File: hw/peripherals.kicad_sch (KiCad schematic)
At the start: 10 parts, among them J4 Expansion, Q2 RU1J002YN, U8 RV-3129-C3, U9 PCA9536D

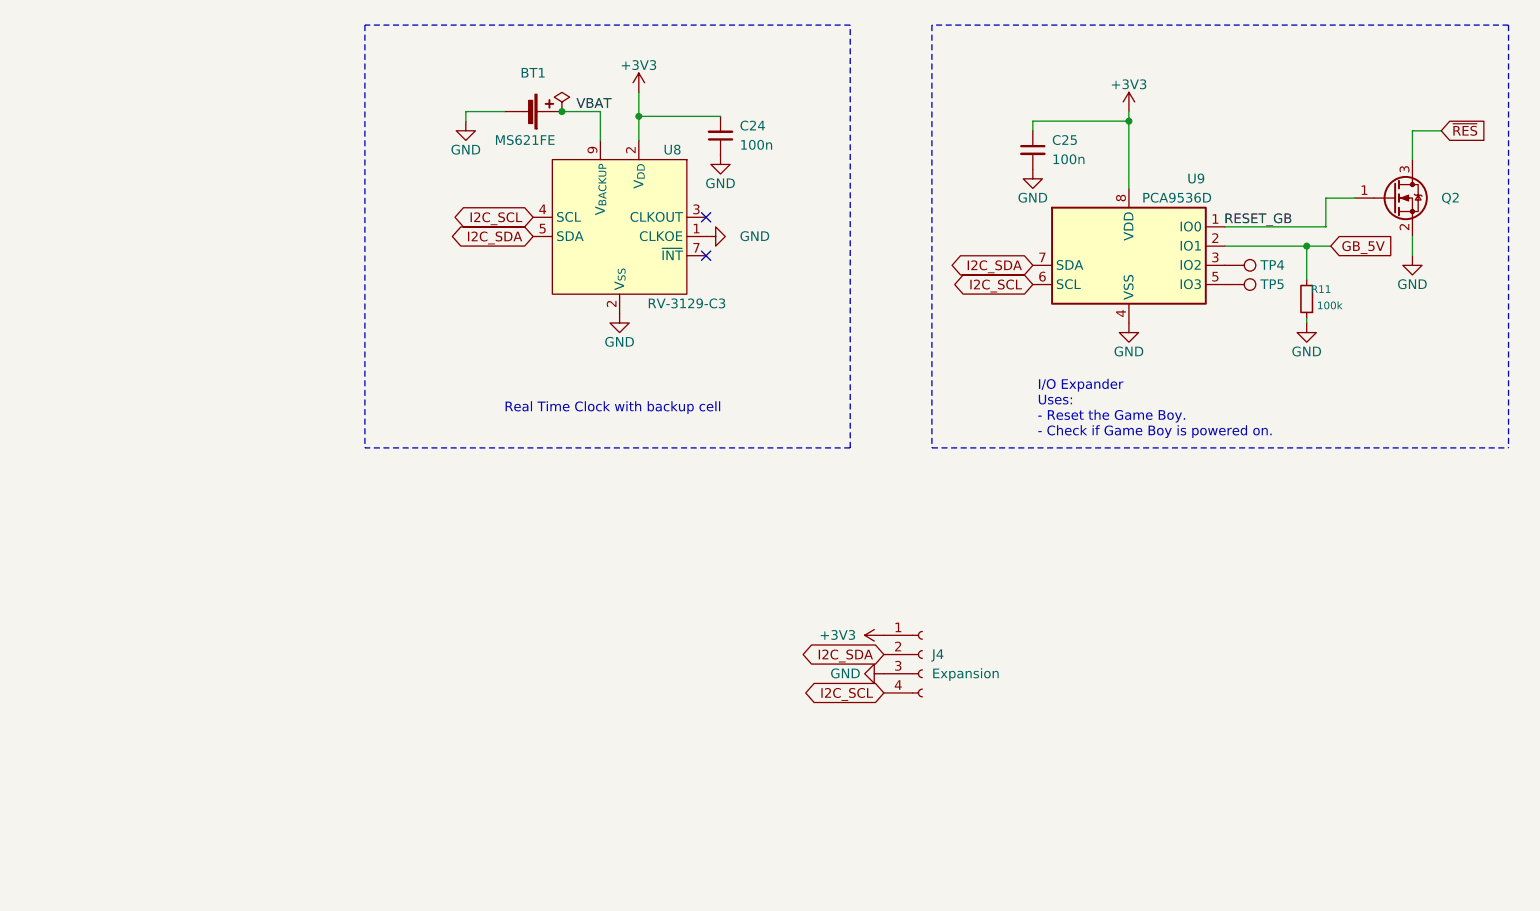
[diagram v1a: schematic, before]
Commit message: hw: use parts from LCSC
Signed-off-by: Mahyar Koshkouei <mk@deltabeard.com>
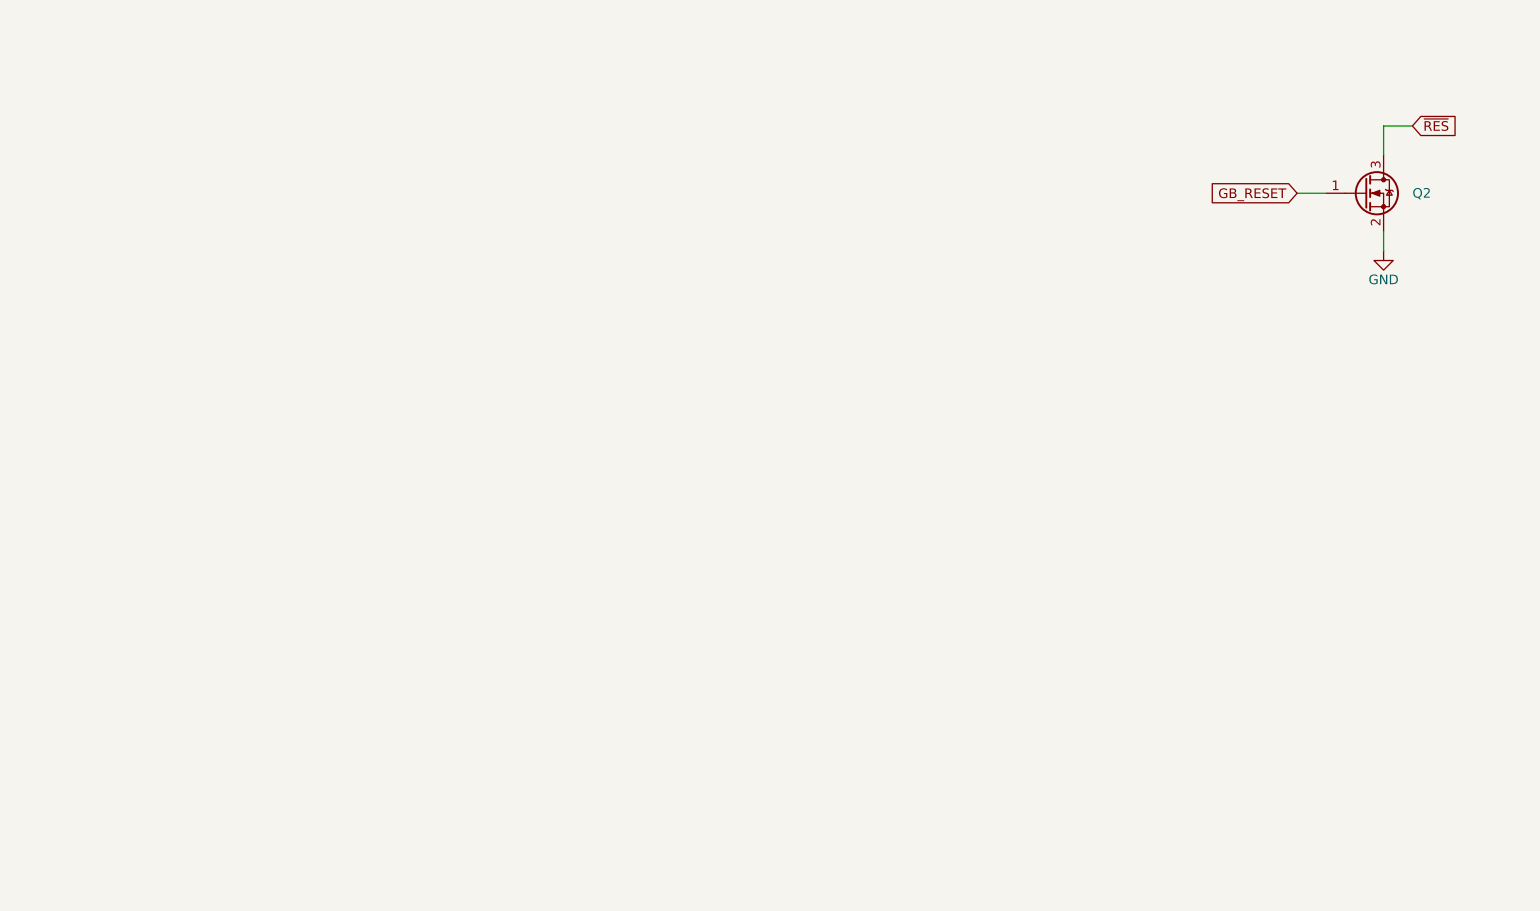
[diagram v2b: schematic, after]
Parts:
- removed BT1: MS621FE, Project_Specific:BatteryHolder_Seiko_MS621FE, symbol Device:Battery_Cell
- removed C24, C25: 100n, Capacitor_SMD:C_0603_1608Metric, symbol Device:C_Small
- removed J4: Expansion, Connector_PinSocket_2.54mm:PinSocket_1x04_P2.54mm_Horizontal, symbol Connector:Conn_01x04_Female
- removed R11: 100k, Resistor_SMD:R_0603_1608Metric, symbol Device:R_Small
- removed TP4: IO2, TestPoint:TestPoint_Pad_D1.5mm, symbol Connector:TestPoint
- removed TP5: IO3, TestPoint:TestPoint_Pad_D1.5mm, symbol Connector:TestPoint
- removed U8: RV-3129-C3, Project_Specific:DFN-10-2.5x2.7mm-P0.8, symbol Project_specific:RV-3129-C3
- removed U9: PCA9536D, Package_SO:SOIC-8_3.9x4.9mm_P1.27mm, symbol Interface_Expansion:PCA9536D
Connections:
- net RESET_GB renamed GB_RESET
- no-connect marks 2 -> 0
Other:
- note removed: "I/O Expander Uses: - Reset the Game Boy. - Check if Game Boy is powered on."
- note removed: "Real Time Clock with backup cell"
- moved on the sheet: Q2

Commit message: hw: complete 2-layer PCB
Signed-off-by: Mahyar Koshkouei <mk@deltabeard.com>
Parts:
- added BT1: Battery_Cell, Project_Specific:BatteryHolder_Seiko_MS621FE, symbol Device:Battery_Cell
- added C23, C24, C25: 100n, Capacitor_SMD:C_0402_1005Metric, symbol Device:C_Small
- added D2: LED, LED_SMD:LED_0603_1608Metric, symbol Device:LED
- added R10, R9: 4k7, Resistor_SMD:R_0402_1005Metric, symbol Device:R_Small
- added R11, R13: 330R, Resistor_SMD:R_0603_1608Metric, symbol Device:R_Small
- added R12: 100k, Resistor_SMD:R_0603_1608Metric, symbol Device:R_Small
- added SW1: SW_SPST, Project_Specific:Push_Button-Horizontal-TC-1109DE-C-J, symbol Switch:SW_SPST
- added U10: MB85RC256VPNF-G-JNERE1, Package_SO:SOIC-8_3.9x4.9mm_P1.27mm, symbol Project_specific:MB85RC256V
- added U8: RV-3129-C3, Project_Specific:SOIC-10_RV-3129-C3, symbol Project_specific:RV-3129-C3
- added U9: PCA9536D, Package_SO:SOIC-8_3.9x4.9mm_P1.27mm, symbol Interface_Expansion:PCA9536D
- Q2: value RU1J002YN -> N-Channel; footprint Package_TO_SOT_SMD:SOT-323_SC-70 -> Package_TO_SOT_SMD:SOT-23; LCSC (none) -> C8545; MFr RU1J002YN -> 2N7002
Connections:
- net GB_RESET: now also R12.1, R13.1, U9.1 (IO0); no longer Q2.1 (G)
- net GND: now also BT1.2 (-), C23.2, C24.2, C25.2, D2.1 (K), SW1.2 (B), U10.1 (A0), U10.2 (A1), U10.3 (A2), U10.4 (GND), U10.7 (WP), U8.1 (CLKOE), U8.2 (V_{SS}), U9.4 (VSS)
- new net: BT1.1 (+), U8.9 (V_{BACKUP})
- new net: SW1.1 (A), U9.2 (IO1)
- new net: R11.1, U9.3 (IO2)
- new net: D2.2 (A), R11.2
- new net: Q2.1 (G), R13.2
- new net +3V3: C23.1, C24.1, C25.1, R10.2, R12.2, R9.2, U10.8 (VDD), U8.2 (V_{SS}), U9.8 (VDD)
- new net I^{2}C_{SCL}: R10.1, U10.6 (SCL), U8.4 (SCL), U9.6 (SCL)
- new net I^{2}C_{SDA}: R9.1, U10.5 (SDA), U8.5 (SDA), U9.7 (SDA)
- no-connect marks 0 -> 3

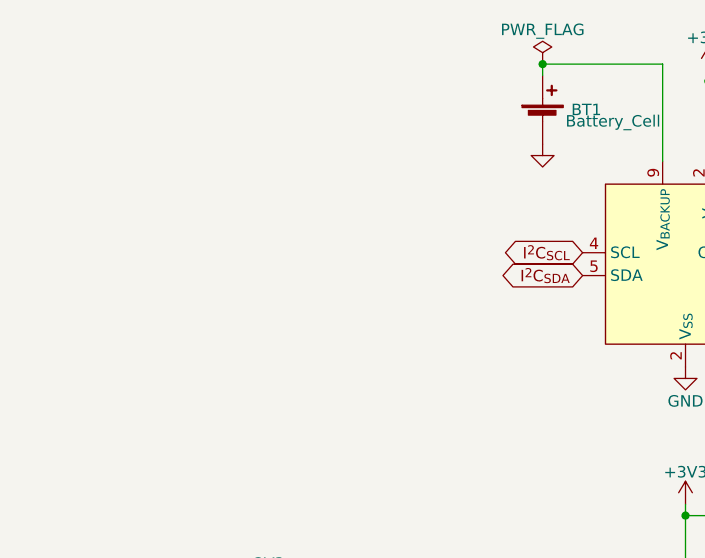
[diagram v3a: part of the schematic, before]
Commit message: hw: replace RTC
Signed-off-by: Mahyar Koshkouei <mk@deltabeard.com>
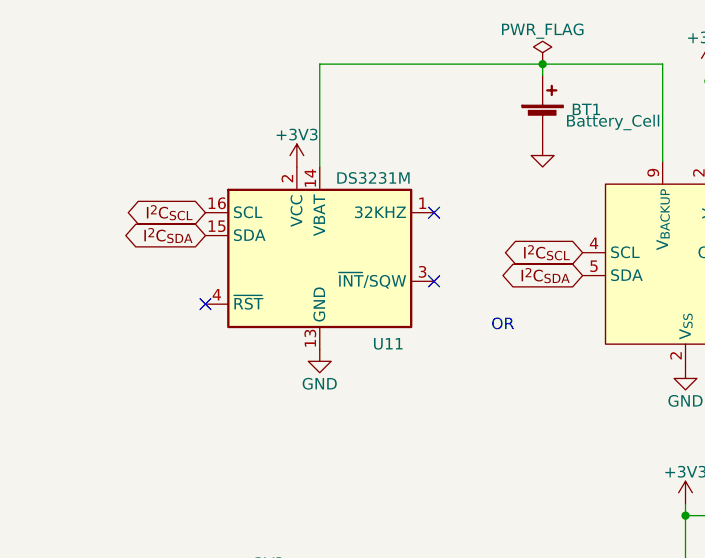
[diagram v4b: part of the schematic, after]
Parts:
- added U11: DS3231M, Package_SO:SOIC-16W_7.5x10.3mm_P1.27mm, symbol Timer_RTC:DS3231M
- U9: LCSC (none) -> C129522
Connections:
- net +3V3: now also U11.2 (VCC)
- net GND: now also U11.10 (GND), U11.11 (GND), U11.12 (GND), U11.13 (GND), U11.5 (GND), U11.6 (GND), U11.7 (GND), U11.8 (GND), U11.9 (GND)
- net I^{2}C_{SCL}: now also U11.16 (SCL)
- net I^{2}C_{SDA}: now also U11.15 (SDA)
- net at BT1.1 (+), U8.9 (V_{BACKUP}): now also U11.14 (VBAT)
- no-connect marks 3 -> 6
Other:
- note added: "OR"
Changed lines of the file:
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@@
   (junction (at 188.595 67.31) (diameter 0.9144) (color 0 0 0 0))
   (junction (at 190.5 100.965) (diameter 0.9144) (color 0 0 0 0))
+  (no_connect (at 46.99 75.565))
+  (no_connect (at 72.39 65.405))
+  (no_connect (at 72.39 73.025))
   (no_connect (at 111.76 69.85))
   (no_connect (at 111.76 74.93))
@@
     (stroke (width 0) (type solid) (color 0 0 0 0))
   )
+  (wire (pts (xy 59.69 48.895) (xy 84.455 48.895))
+    (stroke (width 0) (type solid) (color 0 0 0 0))
+  )
+  (wire (pts (xy 59.69 60.325) (xy 59.69 48.895))
+    (stroke (width 0) (type solid) (color 0 0 0 0))
+  )
   (wire (pts (xy 84.455 48.895) (xy 97.79 48.895))
     (stroke (width 0) (type solid) (color 0 0 0 0))
@@
   (wire (pts (xy 207.01 72.39) (xy 207.01 74.93))
     (stroke (width 0) (type solid) (color 0 0 0 0))
+  )
+  (text "OR" (at 78.74 78.74 0)
+    (effects (font (size 1.27 1.27)) (justify left bottom))
   )
   (global_label "I^{2}C_{SDA}" (shape bidirectional) (at 44.45 118.11 180) (fields_autoplaced)
@@
     )
   )
+  (global_label "I^{2}C_{SCL}" (shape bidirectional) (at 46.99 65.405 180) (fields_autoplaced)
+    (effects (font (size 1.27 1.27)) (justify right))
+    (property "Intersheet References" "${INTERSHEET_REFS}" (id 0) (at 39.0237 65.4844 0)
+      (effects (font (size 1.27 1.27)) (justify right) hide)
+    )
+  )
+  (global_label "I^{2}C_{SDA}" (shape bidirectional) (at 46.99 67.945 180) (fields_autoplaced)
+    (effects (font (size 1.27 1.27)) (justify right))
+    (property "Intersheet References" "${INTERSHEET_REFS}" (id 0) (at 38.9753 68.0244 0)
+      (effects (font (size 1.27 1.27)) (justify right) hide)
+    )
+  )
   (global_label "I^{2}C_{SDA}" (shape bidirectional) (at 87.63 118.11 180) (fields_autoplaced)
     (effects (font (size 1.27 1.27)) (justify right))
@@
     (pin "1")
   )
+  (symbol (lib_id "power:+3V3") (at 57.15 60.325 0) (unit 1)
+    (in_bom yes) (on_board yes) (fields_autoplaced)
+    (property "Reference" "#PWR059" (id 0) (at 57.15 64.135 0)
+      (effects (font (size 1.27 1.27)) hide)
+    )
+    (property "Value" "+3V3" (id 1) (at 57.15 56.769 0))
+    (property "Footprint" "" (id 2) (at 57.15 60.325 0)
+      (effects (font (size 1.27 1.27)) hide)
+    )
+    (property "Datasheet" "" (id 3) (at 57.15 60.325 0)
+      (effects (font (size 1.27 1.27)) hide)
+    )
+    (pin "1")
+  )
   (symbol (lib_id "power:+3V3") (at 100.33 97.79 0) (unit 1)
     (in_bom yes) (on_board yes) (fields_autoplaced)
@@
     )
     (property "Datasheet" "~" (id 3) (at 84.455 48.895 0)
+      (effects (font (size 1.27 1.27)) hide)
+    )
+    (pin "1")
+  )
+  (symbol (lib_id "power:GND") (at 59.69 80.645 0) (unit 1)
+    (in_bom yes) (on_board yes) (fields_autoplaced)
+    (property "Reference" "#PWR060" (id 0) (at 59.69 86.995 0)
+      (effects (font (size 1.27 1.27)) hide)
+    )
+    (property "Value" "GND" (id 1) (at 59.69 84.455 0))
+    (property "Footprint" "" (id 2) (at 59.69 80.645 0)
+      (effects (font (size 1.27 1.27)) hide)
+    )
+    (property "Datasheet" "" (id 3) (at 59.69 80.645 0)
       (effects (font (size 1.27 1.27)) hide)
     )
@@
       (effects (font (size 1.27 1.27)) hide)
     )
+    (property "LCSC" "C129522" (id 4) (at 100.33 115.57 0)
+      (effects (font (size 1.27 1.27)) hide)
+    )
     (pin "1")
     (pin "2")
@@
     (pin "8")
   )
+  (symbol (lib_id "Timer_RTC:DS3231M") (at 59.69 70.485 0) (unit 1)
+    (in_bom yes) (on_board yes)
+    (property "Reference" "U11" (id 0) (at 67.31 80.01 0))
+    (property "Value" "DS3231M" (id 1) (at 69.85 61.595 0)
+      (effects (font (size 1.27 1.27)) (justify right))
+    )
+    (property "Footprint" "Package_SO:SOIC-16W_7.5x10.3mm_P1.27mm" (id 2) (at 59.69 85.725 0)
+      (effects (font (size 1.27 1.27)) hide)
+    )
+    (property "Datasheet" "http://datasheets.maximintegrated.com/en/ds/DS3231.pdf" (id 3) (at 66.548 69.215 0)
+      (effects (font (size 1.27 1.27)) hide)
+    )
+    (property "LCSC" "C37663" (id 4) (at 59.69 70.485 0)
+      (effects (font (size 1.27 1.27)) hide)
+    )
+    (pin "1")
+    (pin "10")
+    (pin "11")
+    (pin "12")
+    (pin "13")
+    (pin "14")
+    (pin "15")
+    (pin "16")
+    (pin "2")
+    (pin "3")
+    (pin "4")
+    (pin "5")
+    (pin "6")
+    (pin "7")
+    (pin "8")
+    (pin "9")
+  )
   (symbol (lib_id "Project_specific:RV-3129-C3") (at 100.33 72.39 0) (unit 1)

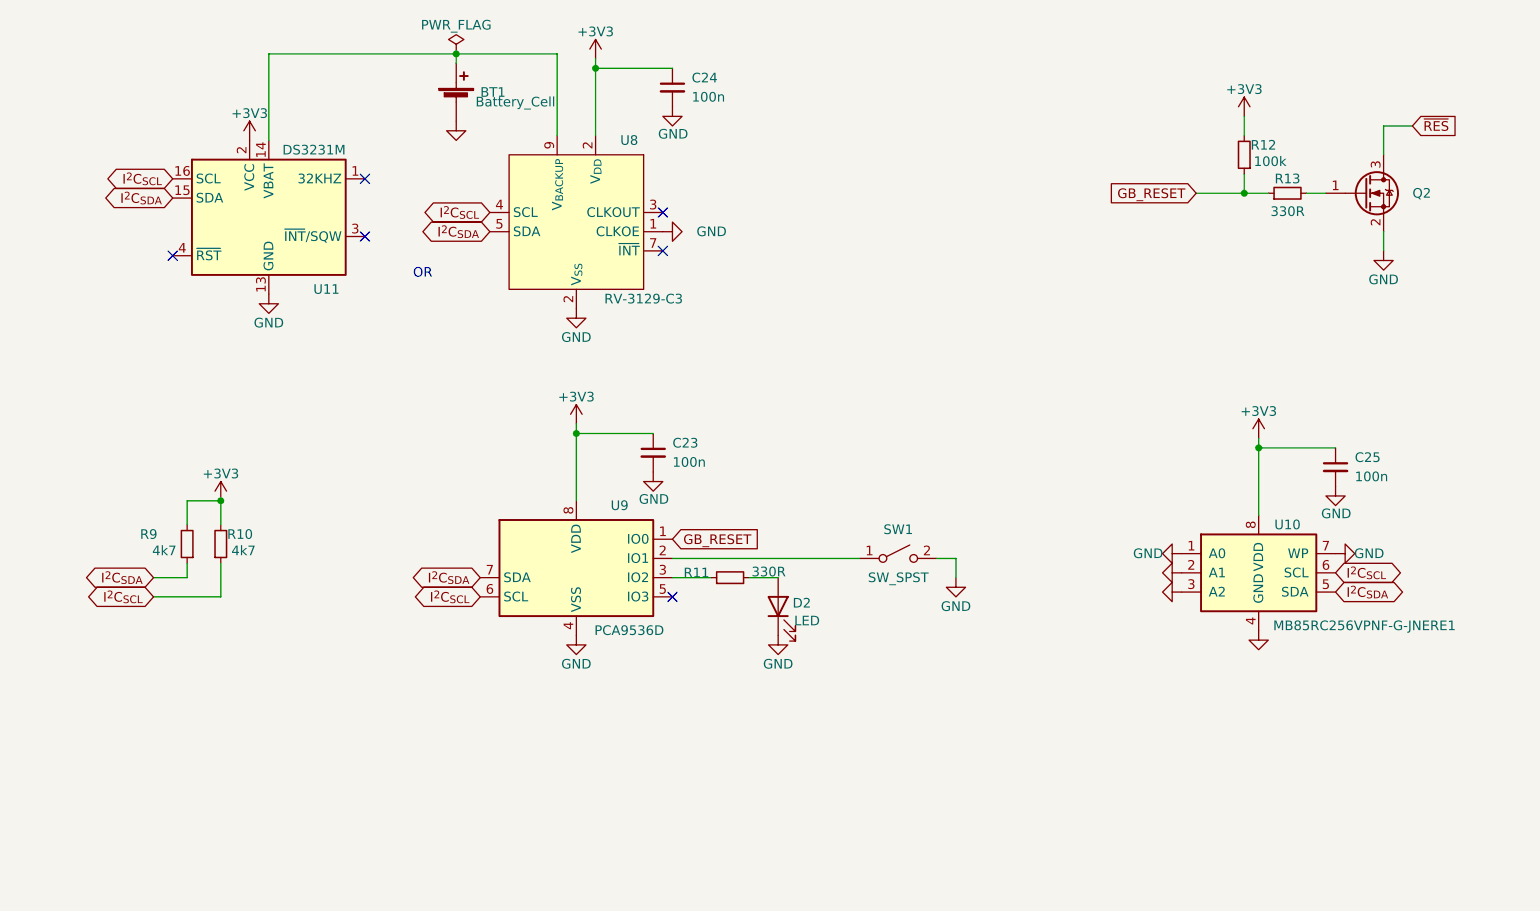
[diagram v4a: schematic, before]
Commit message: hw: complete routing
Use components available on LCSC.

Signed-off-by: Mahyar Koshkouei <mk@deltabeard.com>
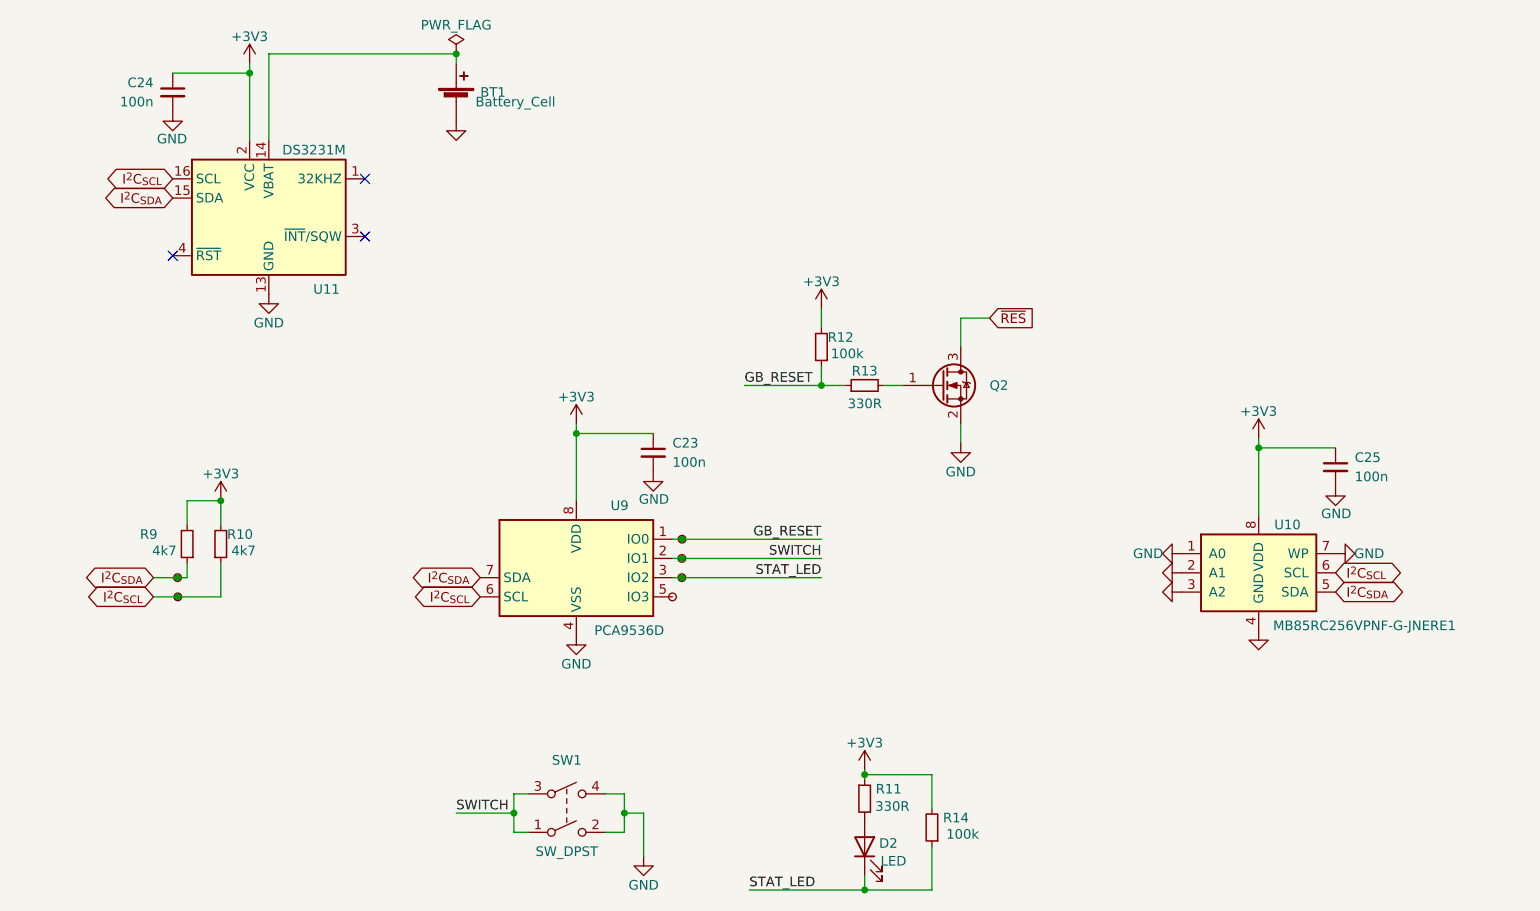
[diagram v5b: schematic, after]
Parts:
- removed SW1: SW_SPST, Project_Specific:Push_Button-Horizontal-TC-1109DE-C-J, symbol Switch:SW_SPST
- removed U8: RV-3129-C3, Project_Specific:SOIC-10_RV-3129-C3, symbol Project_specific:RV-3129-C3
- added R14: 100k, Resistor_SMD:R_0603_1608Metric, symbol Device:R_Small
- added SW1: SW_DPST, Project_Specific:K2-1114SA-A4SW-06, symbol Switch:SW_DPST
- added TP40, TP41, TP42, TP43, TP44, TP45: TestPoint_Small, Project_Specific:TestPoint_Pad_D0.5mm, symbol Connector:TestPoint_Small
- BT1: footprint Project_Specific:BatteryHolder_Seiko_MS621FE -> Battery:BatteryHolder_MPD_BC2003_1x2032; LCSC (none) -> C964835
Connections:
- net +3V3: now also R11.1, R14.2
- net GB_RESET: now also TP45.1
- net GND: now also SW1.2, SW1.4; no longer D2.1 (K)
- net I^{2}C_{SCL}: now also TP41.1
- net I^{2}C_{SDA}: now also TP40.1
- net SWITCH: now reaches U9.2 (IO1)
- net SWITCH: now also SW1.1, SW1.3, TP43.1
- net STAT_LED: now reaches U9.3 (IO2)
- net STAT_LED: now also D2.1 (K), R14.1, TP44.1; no longer R11.1
- net at U9.5 (IO3): now also TP42.1
- no-connect marks 6 -> 3
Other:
- note removed: "OR"
- moved on the sheet: D2, Q2, R11, R12, R13
